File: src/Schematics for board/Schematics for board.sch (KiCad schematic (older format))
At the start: 13 parts

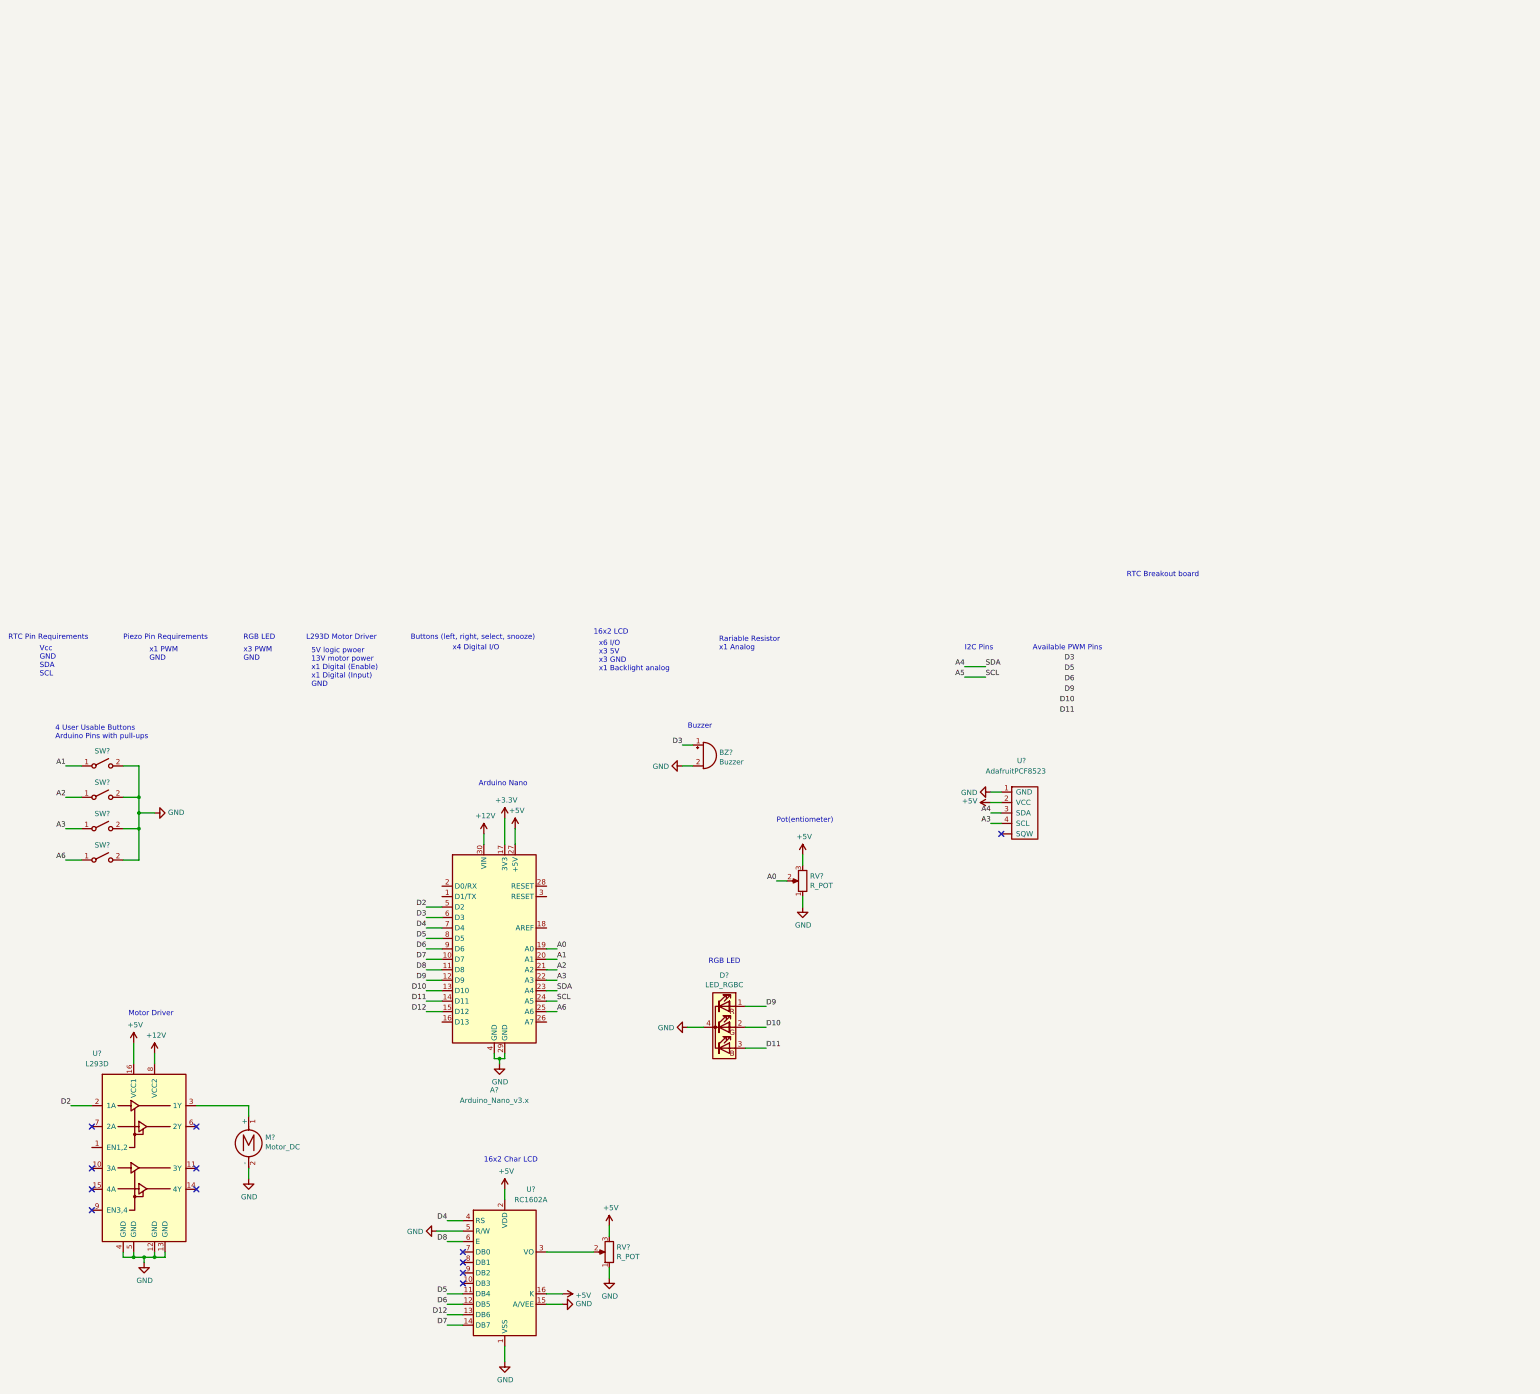
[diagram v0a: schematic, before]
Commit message: changed schematic
included the 4 digit, 7 segment display
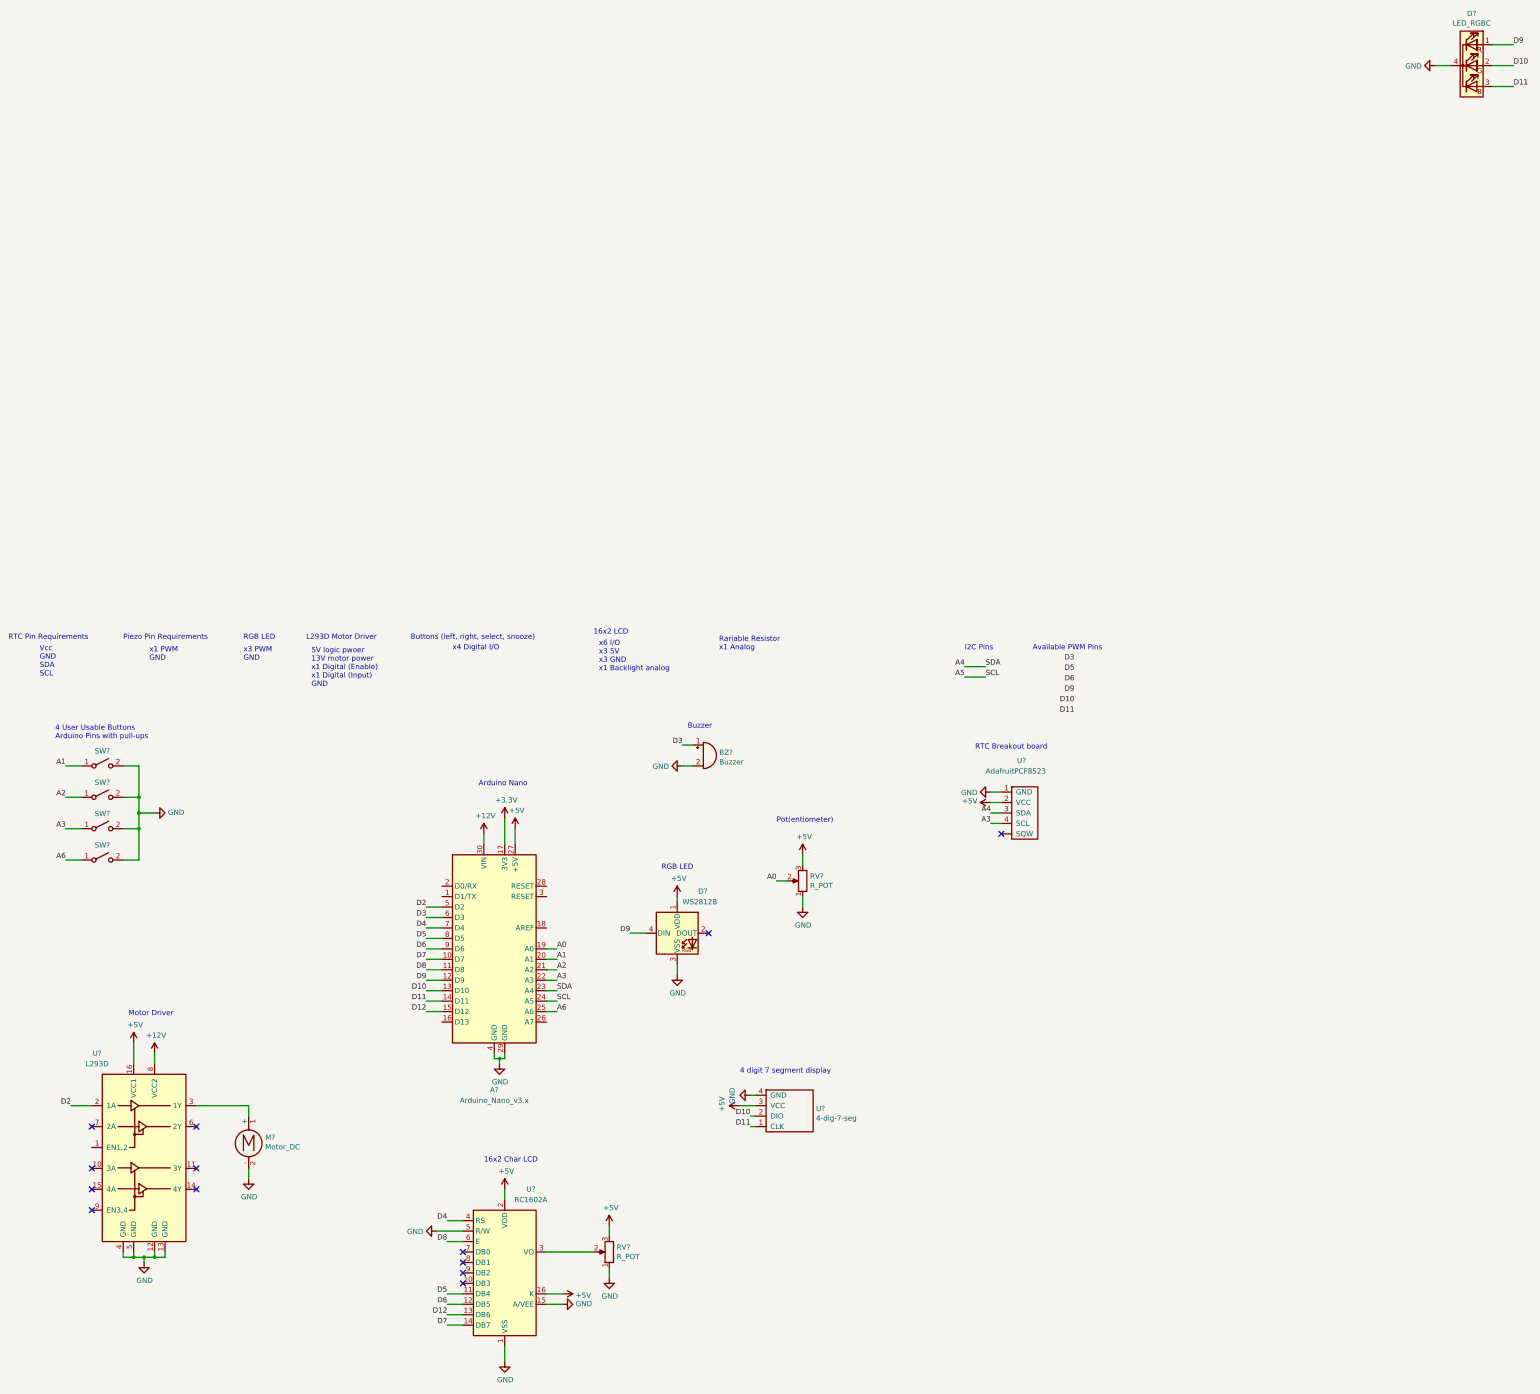
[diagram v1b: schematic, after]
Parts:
- added D?: WS2812B, LED_SMD:LED_WS2812B_PLCC4_5.0x5.0mm_P3.2mm, symbol LED:WS2812B
- added U?: 4-dig-7-seg, symbol Display_Character:4-dig-7-seg
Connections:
- net +5V: now also D?.1 (VDD), U?.3 (VCC)
- net D10: now also U?.2 (DIO)
- net D11: now also U?.1 (CLK)
- net D9: now also D?.4 (DIN)
- net GND: now also D?.3 (VSS), U?.4 (GND)
- no-connect marks 12 -> 13
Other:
- note added: "4 digit 7 segment display"
- moved on the sheet: D?
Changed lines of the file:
@@
 Text Notes 7950 2400 0    50   ~ 0
 Pot(entiometer)
-Text Notes 11300 50   0    50   ~ 0
+Text Notes 9850 1700 0    50   ~ 0
 RTC Breakout board
 Text Notes 1750 4250 0    50   ~ 0
@@
 L Device:LED_RGBC D?
 U 1 1 5E29F059
-P 7450 4350
-F 0 "D?" H 7450 4847 50  0000 C CNN
-F 1 "LED_RGBC" H 7450 4756 50  0000 C CNN
-F 2 "" H 7450 4300 50  0001 C CNN
-F 3 "~" H 7450 4300 50  0001 C CNN
-	1    7450 4350
+P 14600 -4850
+F 0 "D?" H 14600 -4353 50  0000 C CNN
+F 1 "LED_RGBC" H 14600 -4444 50  0000 C CNN
+F 2 "" H 14600 -4900 50  0001 C CNN
+F 3 "~" H 14600 -4900 50  0001 C CNN
+	1    14600 -4850
 	1    0    0    -1
 $EndComp
@@
 L power:GND #PWR?
 U 1 1 5E2A0FE1
-P 7100 4350
-F 0 "#PWR?" H 7100 4100 50  0001 C CNN
-F 1 "GND" V 7105 4222 50  0000 R CNN
-F 2 "" H 7100 4350 50  0001 C CNN
-F 3 "" H 7100 4350 50  0001 C CNN
-	1    7100 4350
-	0    1    1    0
-$EndComp
-Wire Wire Line
-	7100 4350 7250 4350
-Text Label 7850 4150 0    50   ~ 0
+P 14250 -4850
+F 0 "#PWR?" H 14250 -5100 50  0001 C CNN
+F 1 "GND" V 14255 -4978 50  0000 R CNN
+F 2 "" H 14250 -4850 50  0001 C CNN
+F 3 "" H 14250 -4850 50  0001 C CNN
+	1    14250 -4850
+	0    1    1    0
+$EndComp
+Wire Wire Line
+	14250 -4850 14400 -4850
+Text Label 15000 -5050 0    50   ~ 0
 D9
-Text Label 7850 4350 0    50   ~ 0
+Text Label 15000 -4850 0    50   ~ 0
 D10
-Text Label 7850 4550 0    50   ~ 0
+Text Label 15000 -4650 0    50   ~ 0
 D11
 Text Label 4600 3900 2    50   ~ 0
@@
 	4600 4100 4750 4100
 Wire Wire Line
-	7850 4550 7650 4550
-Wire Wire Line
-	7650 4350 7850 4350
-Wire Wire Line
-	7850 4150 7650 4150
+	15000 -4650 14800 -4650
+Wire Wire Line
+	14800 -4850 15000 -4850
+Wire Wire Line
+	15000 -5050 14800 -5050
 Text Label 4600 3500 2    50   ~ 0
 D5
@@
 NoConn ~ 4950 6700
 NoConn ~ 4950 6800
-Text Notes 7300 3750 0    50   ~ 0
+Text Notes 6850 2850 0    50   ~ 0
 RGB LED\n
 $Comp
@@
 Wire Wire Line
 	4600 3700 4750 3700
+$Comp
+L LED:WS2812B D?
+U 1 1 5E237EF2
+P 7000 3450
+F 0 "D?" H 7200 3850 50  0000 L CNN
+F 1 "WS2812B" H 7050 3750 50  0000 L CNN
+F 2 "LED_SMD:LED_WS2812B_PLCC4_5.0x5.0mm_P3.2mm" H 7050 3150 50  0001 L TNN
+F 3 "https://cdn-shop.adafruit.com/datasheets/WS2812B.pdf" H 7100 3075 50  0001 L TNN
+	1    7000 3450
+	1    0    0    -1
+$EndComp
+$Comp
+L power:+5V #PWR?
+U 1 1 5E23B953
+P 7000 3100
+F 0 "#PWR?" H 7000 2950 50  0001 C CNN
+F 1 "+5V" H 7015 3273 50  0000 C CNN
+F 2 "" H 7000 3100 50  0001 C CNN
+F 3 "" H 7000 3100 50  0001 C CNN
+	1    7000 3100
+	1    0    0    -1
+$EndComp
+Wire Wire Line
+	7000 3100 7000 3150
+$Comp
+L power:GND #PWR?
+U 1 1 5E23EF52
+P 7000 3850
+F 0 "#PWR?" H 7000 3600 50  0001 C CNN
+F 1 "GND" H 7005 3677 50  0000 C CNN
+F 2 "" H 7000 3850 50  0001 C CNN
+F 3 "" H 7000 3850 50  0001 C CNN
+	1    7000 3850
+	1    0    0    -1
+$EndComp
+Wire Wire Line
+	7000 3850 7000 3750
+NoConn ~ 7300 3450
+Text Label 6550 3450 2    50   ~ 0
+D9
+Wire Wire Line
+	6550 3450 6700 3450
+$Comp
+L Display_Character:4-dig-7-seg U?
+U 1 1 5E24E4E3
+P 8100 4750
+F 0 "U?" H 8328 4371 50  0000 L CNN
+F 1 "4-dig-7-seg" H 8328 4280 50  0000 L CNN
+F 2 "" H 8100 4750 50  0001 C CNN
+F 3 "" H 8100 4750 50  0001 C CNN
+	1    8100 4750
+	1    0    0    -1
+$EndComp
+Text Notes 7600 4800 0    50   ~ 0
+4 digit 7 segment display
+$Comp
+L power:+5V #PWR?
+U 1 1 5E25304D
+P 7600 5100
+F 0 "#PWR?" H 7600 4950 50  0001 C CNN
+F 1 "+5V" H 7615 5273 50  0000 C CNN
+F 2 "" H 7600 5100 50  0001 C CNN
+F 3 "" H 7600 5100 50  0001 C CNN
+	1    7600 5100
+	0    -1   -1   0
+$EndComp
+Wire Wire Line
+	7600 5100 7750 5100
+$Comp
+L power:GND #PWR?
+U 1 1 5E2560D2
+P 7700 5000
+F 0 "#PWR?" H 7700 4750 50  0001 C CNN
+F 1 "GND" H 7705 4827 50  0000 C CNN
+F 2 "" H 7700 5000 50  0001 C CNN
+F 3 "" H 7700 5000 50  0001 C CNN
+	1    7700 5000
+	0    1    1    0
+$EndComp
+Wire Wire Line
+	7700 5000 7750 5000
+Text Label 7700 5200 2    50   ~ 0
+D10
+Text Label 7700 5300 2    50   ~ 0
+D11
+Wire Wire Line
+	7700 5200 7750 5200
+Wire Wire Line
+	7750 5300 7700 5300
 $EndSCHEMATC

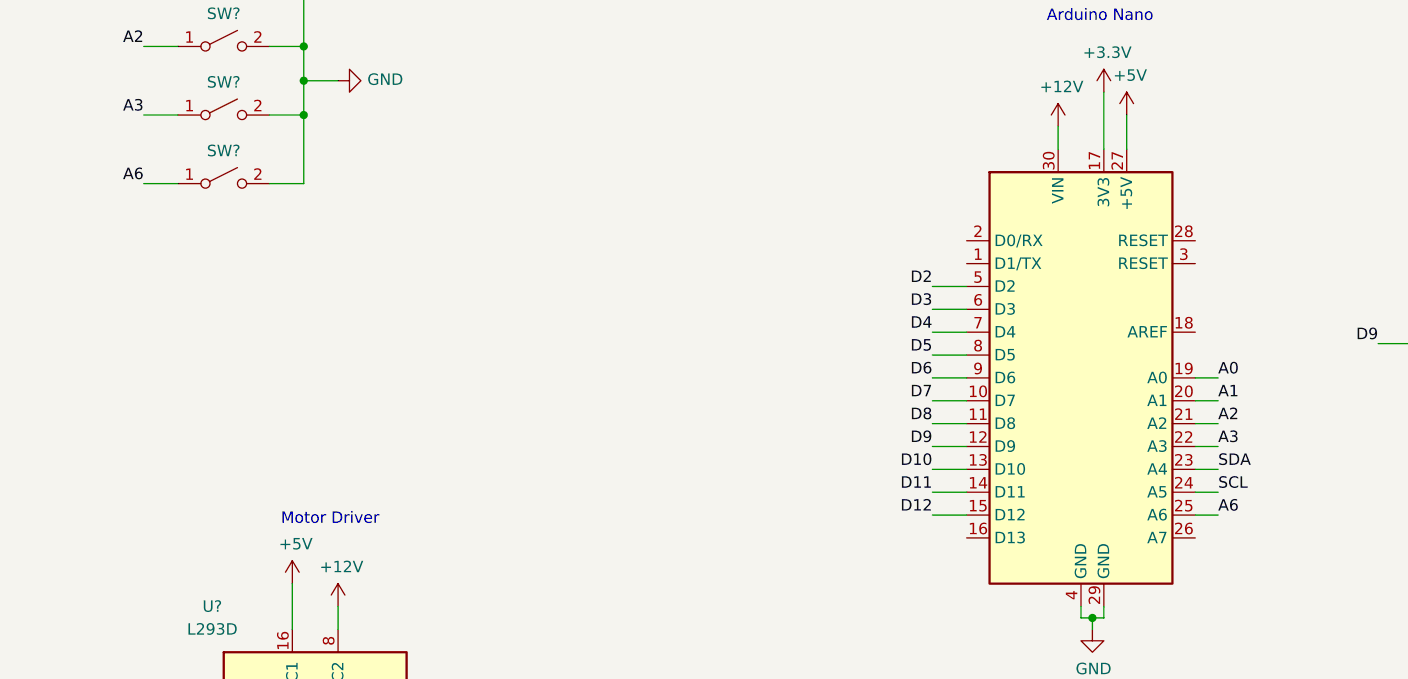
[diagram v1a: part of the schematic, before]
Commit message: fixed A6 problem
A6 is Analog input ONLY, so swapped to D1 (TX) instead
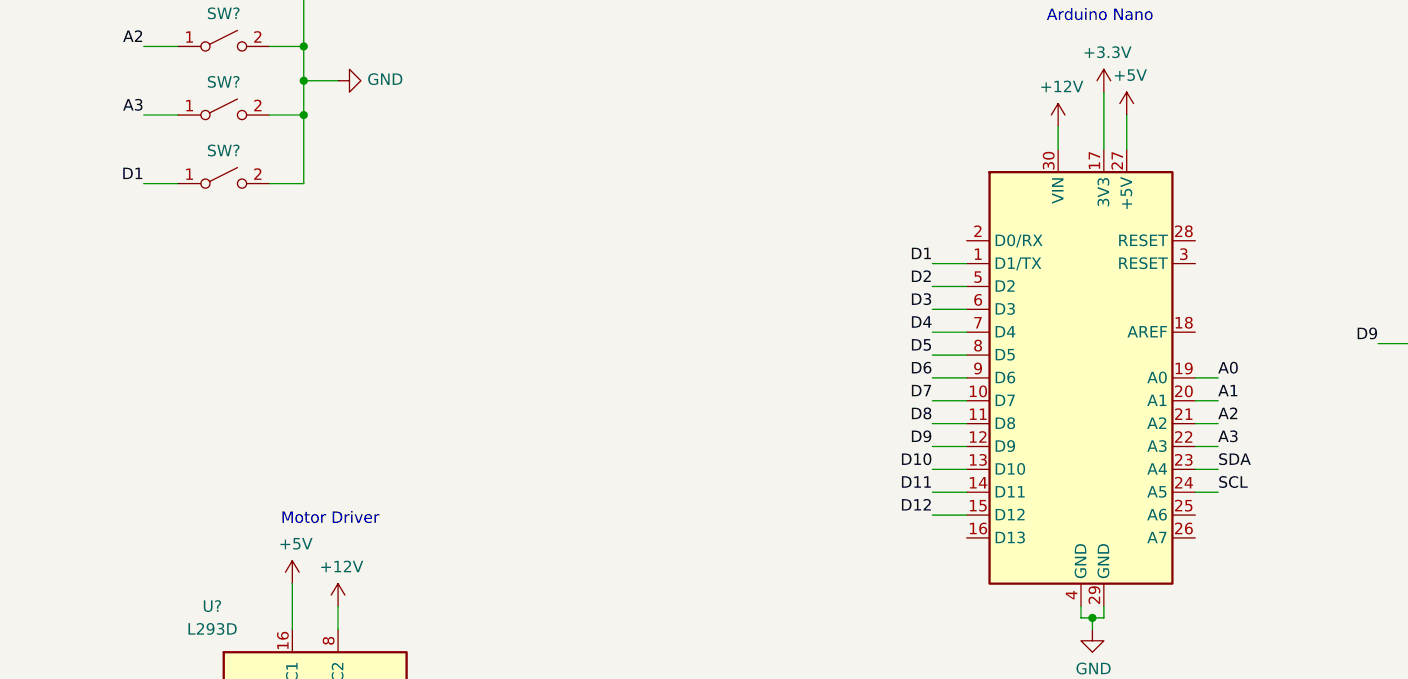
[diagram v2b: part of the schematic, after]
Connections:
- net D1: now reaches A?.1 (D1/TX)
- net D1: now also SW?.1 (A)
- net A6: no longer names the net of A?.25 (A6)
- net A6: no longer SW?.1 (A)
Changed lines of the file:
@@
 Text Label 1150 2450 2    50   ~ 0
 A3
-Text Label 1150 2750 2    50   ~ 0
-A6
 Wire Wire Line
 	1150 1850 1300 1850
@@
 Text Label 5850 3900 0    50   ~ 0
 A3
-Text Label 5850 4200 0    50   ~ 0
-A6
 Wire Wire Line
 	5850 3700 5750 3700
@@
 Wire Wire Line
 	5850 4100 5750 4100
-Wire Wire Line
-	5750 4200 5850 4200
 $Comp
 L Display_Character:RC1602A U?
@@
 Wire Wire Line
 	7750 5300 7700 5300
+Text Label 4600 3100 2    50   ~ 0
+D1
+Wire Wire Line
+	4600 3100 4750 3100
+Text Label 1150 2750 2    50   ~ 0
+D1
 $EndSCHEMATC

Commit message: schematic updates
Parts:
- removed D?: WS2812B, LED_SMD:LED_WS2812B_PLCC4_5.0x5.0mm_P3.2mm, symbol LED:WS2812B
- added D?: LED, symbol Device:LED
- added JP?: Water Detector, symbol Jumper:SolderJumper_2_Open
- added R?: 10k, symbol Device:R_US
- added R?: 220, symbol Device:R_US
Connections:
- net +5V: now also R?.2
- net D9: now also R?.1
- net GND: now also D?.1 (K), JP?.1 (A)
- net A6: now reaches A?.25 (A6)
- net A6: now also JP?.2 (B), R?.1
- new net: D?.2 (A), R?.2
- no-connect marks 13 -> 12
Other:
- note removed: "RGB LED\n"
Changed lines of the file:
@@
 NoConn ~ 4950 6700
 NoConn ~ 4950 6800
-Text Notes 6850 2850 0    50   ~ 0
-RGB LED\n
 $Comp
 L power:GND #PWR?
@@
 Wire Wire Line
 	4600 3700 4750 3700
-$Comp
-L LED:WS2812B D?
-U 1 1 5E237EF2
-P 7000 3450
-F 0 "D?" H 7200 3850 50  0000 L CNN
-F 1 "WS2812B" H 7050 3750 50  0000 L CNN
-F 2 "LED_SMD:LED_WS2812B_PLCC4_5.0x5.0mm_P3.2mm" H 7050 3150 50  0001 L TNN
-F 3 "https://cdn-shop.adafruit.com/datasheets/WS2812B.pdf" H 7100 3075 50  0001 L TNN
-	1    7000 3450
-	1    0    0    -1
-$EndComp
-$Comp
-L power:+5V #PWR?
-U 1 1 5E23B953
-P 7000 3100
-F 0 "#PWR?" H 7000 2950 50  0001 C CNN
-F 1 "+5V" H 7015 3273 50  0000 C CNN
-F 2 "" H 7000 3100 50  0001 C CNN
-F 3 "" H 7000 3100 50  0001 C CNN
-	1    7000 3100
-	1    0    0    -1
-$EndComp
-Wire Wire Line
-	7000 3100 7000 3150
-$Comp
-L power:GND #PWR?
-U 1 1 5E23EF52
-P 7000 3850
-F 0 "#PWR?" H 7000 3600 50  0001 C CNN
-F 1 "GND" H 7005 3677 50  0000 C CNN
-F 2 "" H 7000 3850 50  0001 C CNN
-F 3 "" H 7000 3850 50  0001 C CNN
-	1    7000 3850
-	1    0    0    -1
-$EndComp
-Wire Wire Line
-	7000 3850 7000 3750
-NoConn ~ 7300 3450
 Text Label 6550 3450 2    50   ~ 0
 D9
@@
 Text Label 1150 2750 2    50   ~ 0
 D1
+Text Label 5850 4200 0    50   ~ 0
+A6
+$Comp
+L Device:LED D?
+U 1 1 5E2803D6
+P 7250 3450
+F 0 "D?" H 7243 3195 50  0000 C CNN
+F 1 "LED" H 7243 3286 50  0000 C CNN
+F 2 "" H 7250 3450 50  0001 C CNN
+F 3 "~" H 7250 3450 50  0001 C CNN
+	1    7250 3450
+	-1   0    0    1
+$EndComp
+$Comp
+L Device:R_US R?
+U 1 1 5E2819D2
+P 6850 3450
+F 0 "R?" V 6750 3450 50  0000 C CNN
+F 1 "220" V 6650 3450 50  0000 C CNN
+F 2 "" V 6890 3440 50  0001 C CNN
+F 3 "~" H 6850 3450 50  0001 C CNN
+	1    6850 3450
+	0    -1   -1   0
+$EndComp
+$Comp
+L power:GND #PWR?
+U 1 1 5E28244E
+P 7500 3450
+F 0 "#PWR?" H 7500 3200 50  0001 C CNN
+F 1 "GND" H 7505 3277 50  0000 C CNN
+F 2 "" H 7500 3450 50  0001 C CNN
+F 3 "" H 7500 3450 50  0001 C CNN
+	1    7500 3450
+	0    -1   -1   0
+$EndComp
+Wire Wire Line
+	7000 3450 7100 3450
+Wire Wire Line
+	7400 3450 7500 3450
+Wire Wire Line
+	6350 4850 6250 4850
+Wire Wire Line
+	6750 4850 6650 4850
+$Comp
+L power:GND #PWR?
+U 1 1 5E274064
+P 6250 4850
+F 0 "#PWR?" H 6250 4600 50  0001 C CNN
+F 1 "GND" H 6255 4677 50  0000 C CNN
+F 2 "" H 6250 4850 50  0001 C CNN
+F 3 "" H 6250 4850 50  0001 C CNN
+	1    6250 4850
+	0    1    1    0
+$EndComp
+Text Label 6750 4850 0    50   ~ 0
+A6
+Wire Wire Line
+	5750 4200 6100 4200
+$Comp
+L Jumper:SolderJumper_2_Open JP?
+U 1 1 5E26DABC
+P 6500 4850
+F 0 "JP?" H 6500 5055 50  0000 C CNN
+F 1 "Water Detector" H 6500 4964 50  0000 C CNN
+F 2 "" H 6500 4850 50  0001 C CNN
+F 3 "~" H 6500 4850 50  0001 C CNN
+	1    6500 4850
+	1    0    0    -1
+$EndComp
+Wire Wire Line
+	6500 4200 6400 4200
+$Comp
+L power:+5V #PWR?
+U 1 1 5E26964A
+P 6500 4200
+F 0 "#PWR?" H 6500 4050 50  0001 C CNN
+F 1 "+5V" H 6515 4373 50  0000 C CNN
+F 2 "" H 6500 4200 50  0001 C CNN
+F 3 "" H 6500 4200 50  0001 C CNN
+	1    6500 4200
+	0    1    1    0
+$EndComp
+$Comp
+L Device:R_US R?
+U 1 1 5E261E28
+P 6250 4200
+F 0 "R?" V 6150 4200 50  0000 C CNN
+F 1 "10k" V 6050 4200 50  0000 C CNN
+F 2 "" V 6290 4190 50  0001 C CNN
+F 3 "~" H 6250 4200 50  0001 C CNN
+	1    6250 4200
+	0    -1   -1   0
+$EndComp
 $EndSCHEMATC
